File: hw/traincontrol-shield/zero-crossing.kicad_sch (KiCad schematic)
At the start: 3 parts, among them U2 H11AA1

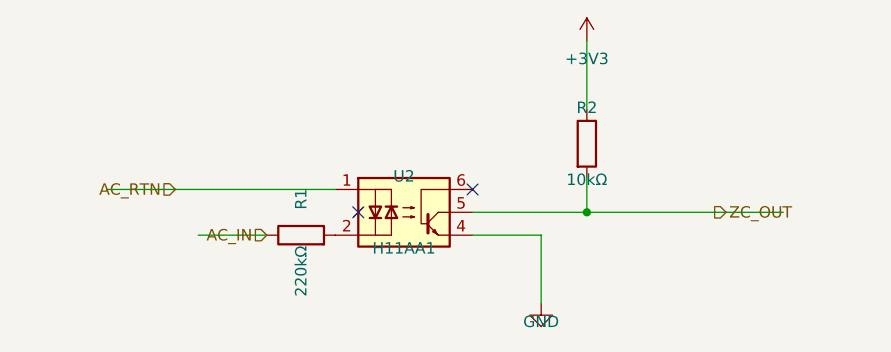
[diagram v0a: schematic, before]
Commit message: Fix hlabel placement: label sits at stub outer end (lx), not pin tip (x)
The hierarchical label connection point must be at lx (the outer end of
the stub wire), not at x (the IC pin tip). With the label at x, it was
overlapping the pin itself instead of sitting at the end of the routing
stub where it belongs.

  angle=180 (left-side): lx = x - STUB  → label to the left of pin ✓
  angle=0   (right-side): lx = x + STUB  → label to the right of pin ✓

Wire still runs x↔lx, connecting the IC pin to the label connection.
Updated gen_all_sheets.py and gen_power_supply.py.

Co-Authored-By: Claude Sonnet 4.6 <noreply@anthropic.com>
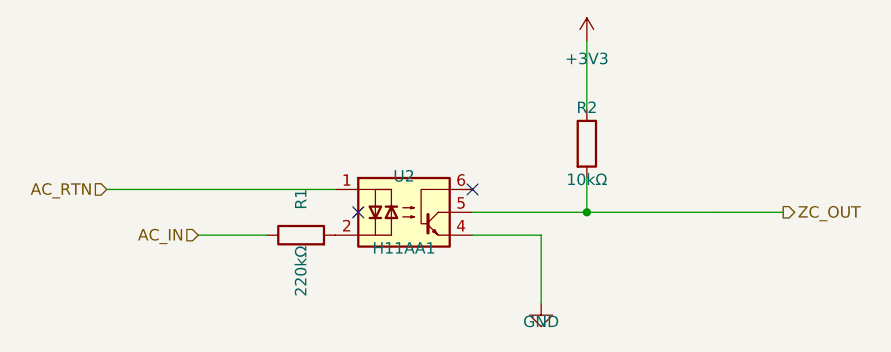
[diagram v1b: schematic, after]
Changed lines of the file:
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@@
 	(hierarchical_label "AC_IN"
 		(shape input)
-		(at 81.28 92.71 180)
+		(at 73.66 92.71 180)
 		(fields_autoplaced yes)
 		(effects (font (size 1.27 1.27)) (justify right bottom))
 		(property "Intersheetrefs" "${INTERSHEET_REFS}"
-			(at 81.28 92.71 0)
+			(at 73.66 92.71 0)
 			(effects (font (size 1.27 1.27)) (hide yes))
 		)
@@
 	(hierarchical_label "AC_RTN"
 		(shape input)
-		(at 71.12 87.63 180)
+		(at 63.50000000000001 87.63 180)
 		(fields_autoplaced yes)
 		(effects (font (size 1.27 1.27)) (justify right bottom))
 		(property "Intersheetrefs" "${INTERSHEET_REFS}"
-			(at 71.12 87.63 0)
+			(at 63.50000000000001 87.63 0)
 			(effects (font (size 1.27 1.27)) (hide yes))
 		)
@@
 	(hierarchical_label "ZC_OUT"
 		(shape output)
-		(at 131.04 90.17 0)
+		(at 138.66 90.17 0)
 		(fields_autoplaced yes)
 		(effects (font (size 1.27 1.27)) (justify left bottom))
 		(property "Intersheetrefs" "${INTERSHEET_REFS}"
-			(at 131.04 90.17 0)
+			(at 138.66 90.17 0)
 			(effects (font (size 1.27 1.27)) (hide yes))
 		)

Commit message: Increase component spacing to eliminate pin-wire overlaps
- zero-crossing: move R1 left 7.62mm, add bridge wire to U2 pin2
- xor-interlock: move C10 right of U3 output (76→91mm), move C11 right (168→178mm)
- opto-triac: add 7.62mm COMP_GAP between MOC3021 and LED/gate resistors
- triacs-snubbers: move snubber column right (99→109mm), add 7.62mm gap between R and C
- mcu: widen C4/C5/C6 decap spacing from 7.62mm to 10.16mm
- power-supply: move R13 down 7.62mm, add bridge wire to R12

Co-Authored-By: Claude Sonnet 4.6 <noreply@anthropic.com>
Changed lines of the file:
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@@
 	(symbol
 		(lib_id "Device:R")
-		(at 85.09 92.71 90)
+		(at 77.47 92.71 90)
 		(unit 1)
 		(exclude_from_sim no)
@@
 		(dnp no)
 		(property "Reference" "R1"
-			(at 85.09 88.71 0)
+			(at 77.47 88.71 0)
 			(effects (font (size 1.27 1.27)))
 		)
 		(property "Value" "220kΩ"
-			(at 85.09 96.71 0)
+			(at 77.47 96.71 0)
 			(effects (font (size 1.27 1.27)))
 		)
 		(property "Footprint" "Resistor_SMD:R_0603_1608Metric"
-			(at 85.09 92.71 0)
+			(at 77.47 92.71 0)
 			(effects (font (size 1.27 1.27)) (hide yes))
 		)
 		(property "Datasheet" "~"
-			(at 85.09 92.71 0)
+			(at 77.47 92.71 0)
 			(effects (font (size 1.27 1.27)) (hide yes))
 		)
@@
 			)
 		)
+	)
+	(wire
+		(pts (xy 81.28 92.71) (xy 88.9 92.71))
+		(stroke (width 0) (type solid))
 	)
 	(symbol
@@
 	)
 	(wire
-		(pts (xy 73.66 92.71) (xy 81.28 92.71))
+		(pts (xy 66.03999999999999 92.71) (xy 73.66 92.71))
 		(stroke (width 0) (type solid))
 	)
 	(hierarchical_label "AC_IN"
 		(shape input)
-		(at 73.66 92.71 180)
+		(at 66.03999999999999 92.71 180)
 		(fields_autoplaced yes)
 		(effects (font (size 1.27 1.27)) (justify right bottom))
 		(property "Intersheetrefs" "${INTERSHEET_REFS}"
-			(at 73.66 92.71 0)
+			(at 66.03999999999999 92.71 0)
 			(effects (font (size 1.27 1.27)) (hide yes))
 		)

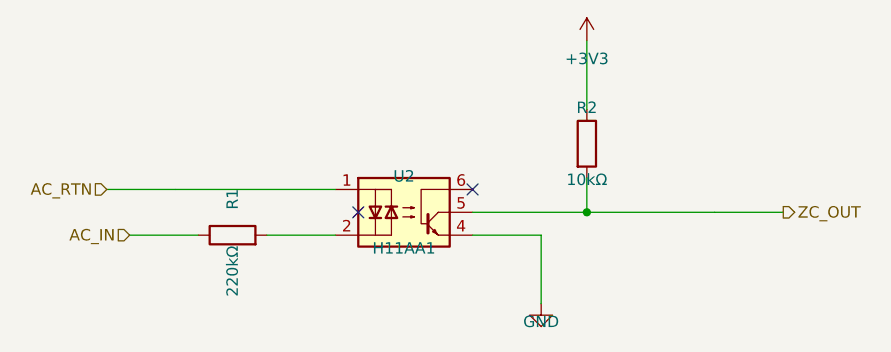
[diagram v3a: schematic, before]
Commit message: Enforce IC-to-passive body gap ≥ 2×STUB across all sheets
Computed symbol body extents from KiCad library and applied:
  IC-to-IC gap  = 4×STUB = 30.48mm between body edges
  IC-to-passive = 2×STUB = 15.24mm between body edges

Violations found and fixed:
- zero-crossing: R1 center 77.47→73.66mm (R1 body right→U2 body left = 15.24mm ✓)
- zero-crossing: R2 center 116.84→119.38mm (U2 body right→R2 body left = 16.76mm ✓)
- opto-triac: COMP_GAP 7.62→15.24mm (MOC body edge to R body edge = 19.05mm ✓)

All other spacings were already compliant (xor-interlock U3→U4 50.8mm,
triacs-snubbers TRIAC→R-sn 18mm, power-supply D1→C1 38mm).

Co-Authored-By: Claude Sonnet 4.6 <noreply@anthropic.com>
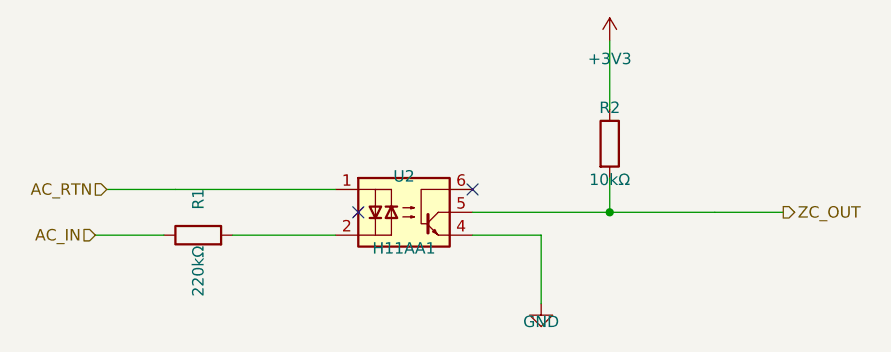
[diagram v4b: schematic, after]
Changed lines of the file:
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@@
 	(symbol
 		(lib_id "Device:R")
-		(at 77.47 92.71 90)
+		(at 73.66 92.71 90)
 		(unit 1)
 		(exclude_from_sim no)
@@
 		(dnp no)
 		(property "Reference" "R1"
-			(at 77.47 88.71 0)
+			(at 73.66 88.71 0)
 			(effects (font (size 1.27 1.27)))
 		)
 		(property "Value" "220kΩ"
-			(at 77.47 96.71 0)
+			(at 73.66 96.71 0)
 			(effects (font (size 1.27 1.27)))
 		)
 		(property "Footprint" "Resistor_SMD:R_0603_1608Metric"
-			(at 77.47 92.71 0)
+			(at 73.66 92.71 0)
 			(effects (font (size 1.27 1.27)) (hide yes))
 		)
 		(property "Datasheet" "~"
-			(at 77.47 92.71 0)
+			(at 73.66 92.71 0)
 			(effects (font (size 1.27 1.27)) (hide yes))
 		)
@@
 	)
 	(wire
-		(pts (xy 81.28 92.71) (xy 88.9 92.71))
+		(pts (xy 77.47 92.71) (xy 88.9 92.71))
 		(stroke (width 0) (type solid))
 	)
 	(symbol
 		(lib_id "Device:R")
-		(at 116.84 82.55 0)
+		(at 119.38 82.55 0)
 		(unit 1)
 		(exclude_from_sim no)
@@
 		(dnp no)
 		(property "Reference" "R2"
-			(at 116.84 78.55 0)
+			(at 119.38 78.55 0)
 			(effects (font (size 1.27 1.27)))
 		)
 		(property "Value" "10kΩ"
-			(at 116.84 86.55 0)
+			(at 119.38 86.55 0)
 			(effects (font (size 1.27 1.27)))
 		)
 		(property "Footprint" "Resistor_SMD:R_0603_1608Metric"
-			(at 116.84 82.55 0)
+			(at 119.38 82.55 0)
 			(effects (font (size 1.27 1.27)) (hide yes))
 		)
 		(property "Datasheet" "~"
-			(at 116.84 82.55 0)
+			(at 119.38 82.55 0)
 			(effects (font (size 1.27 1.27)) (hide yes))
 		)
@@
 	)
 	(wire
-		(pts (xy 116.84 78.74) (xy 116.84 71.11999999999999))
+		(pts (xy 119.38 78.74) (xy 119.38 71.11999999999999))
 		(stroke (width 0) (type solid))
 	)
 	(symbol
 		(lib_id "power:+3V3")
-		(at 116.84 71.11999999999999 0)
+		(at 119.38 71.11999999999999 0)
 		(unit 1)
 		(exclude_from_sim no)
@@
 		(dnp no)
 		(property "Reference" "#PWR0302"
-			(at 116.84 69.11999999999999 0)
+			(at 119.38 69.11999999999999 0)
 			(effects (font (size 1.27 1.27)) (hide yes))
 		)
 		(property "Value" "+3V3"
-			(at 116.84 73.11999999999999 0)
+			(at 119.38 73.11999999999999 0)
 			(effects (font (size 1.27 1.27)))
 		)
 		(property "Footprint" ""
-			(at 116.84 71.11999999999999 0)
+			(at 119.38 71.11999999999999 0)
 			(effects (font (size 1.27 1.27)) (hide yes))
 		)
 		(property "Datasheet" ""
-			(at 116.84 71.11999999999999 0)
+			(at 119.38 71.11999999999999 0)
 			(effects (font (size 1.27 1.27)) (hide yes))
 		)
@@
 	)
 	(wire
-		(pts (xy 116.84 86.36) (xy 116.84 90.17))
-		(stroke (width 0) (type solid))
-	)
-	(wire
-		(pts (xy 116.84 90.17) (xy 104.14 90.17))
-		(stroke (width 0) (type solid))
-	)
-	(wire
-		(pts (xy 116.84 90.17) (xy 131.04 90.17))
+		(pts (xy 119.38 86.36) (xy 119.38 90.17))
+		(stroke (width 0) (type solid))
+	)
+	(wire
+		(pts (xy 119.38 90.17) (xy 104.14 90.17))
+		(stroke (width 0) (type solid))
+	)
+	(wire
+		(pts (xy 119.38 90.17) (xy 131.04 90.17))
 		(stroke (width 0) (type solid))
 	)
@@
 	)
 	(wire
-		(pts (xy 66.03999999999999 92.71) (xy 73.66 92.71))
+		(pts (xy 62.23 92.71) (xy 69.85 92.71))
 		(stroke (width 0) (type solid))
 	)
 	(hierarchical_label "AC_IN"
 		(shape input)
-		(at 66.03999999999999 92.71 180)
+		(at 62.23 92.71 180)
 		(fields_autoplaced yes)
 		(effects (font (size 1.27 1.27)) (justify right bottom))
 		(property "Intersheetrefs" "${INTERSHEET_REFS}"
-			(at 66.03999999999999 92.71 0)
+			(at 62.23 92.71 0)
 			(effects (font (size 1.27 1.27)) (hide yes))
 		)
@@
 	)
 	(junction
-		(at 116.84 90.17)
+		(at 119.38 90.17)
 		(diameter 0)
 		(color 0 0 0 0)
